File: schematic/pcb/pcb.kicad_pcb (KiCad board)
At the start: 2 copper layers, 23 parts, among them P1 USB_C_Plug_USB2.0, U1 ESP32-WROOM-32, U2 NEO-M9N, U3 CP2102N-Axx-xQFN28

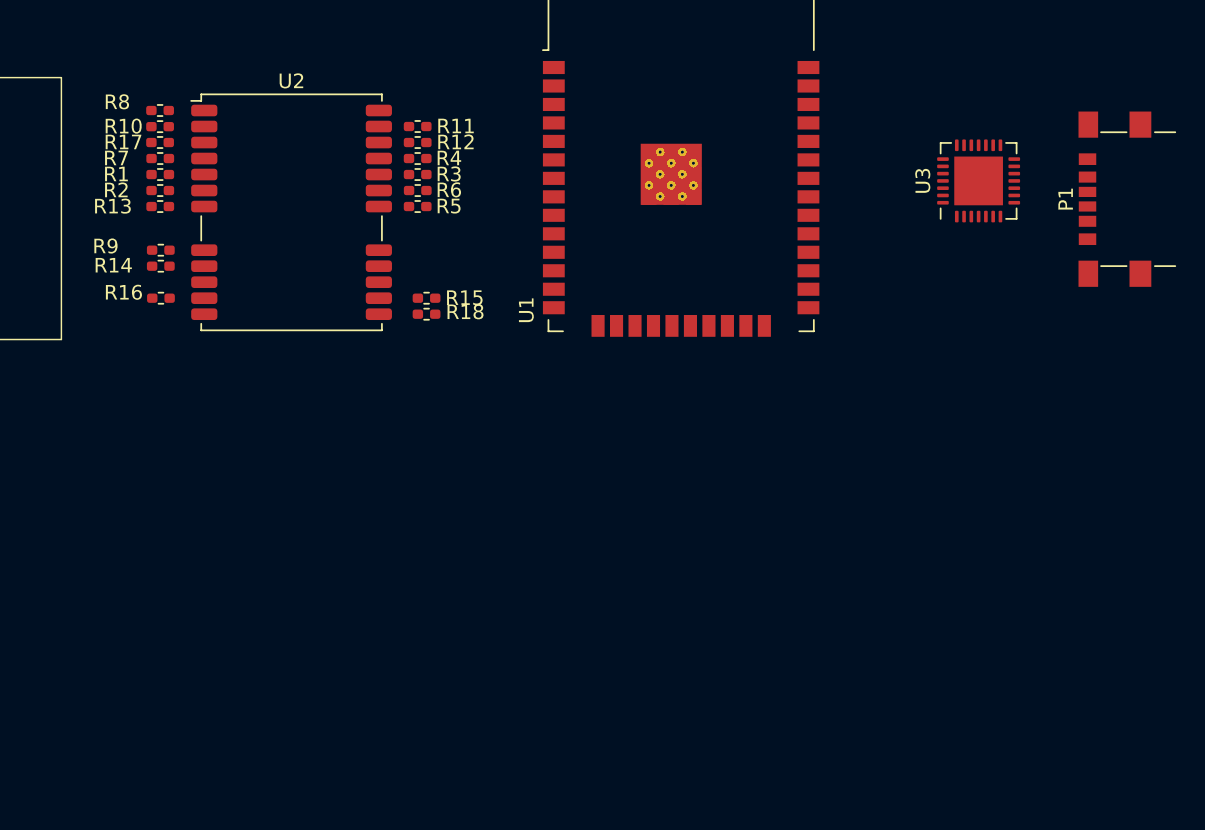
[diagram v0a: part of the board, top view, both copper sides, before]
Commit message: schematic update
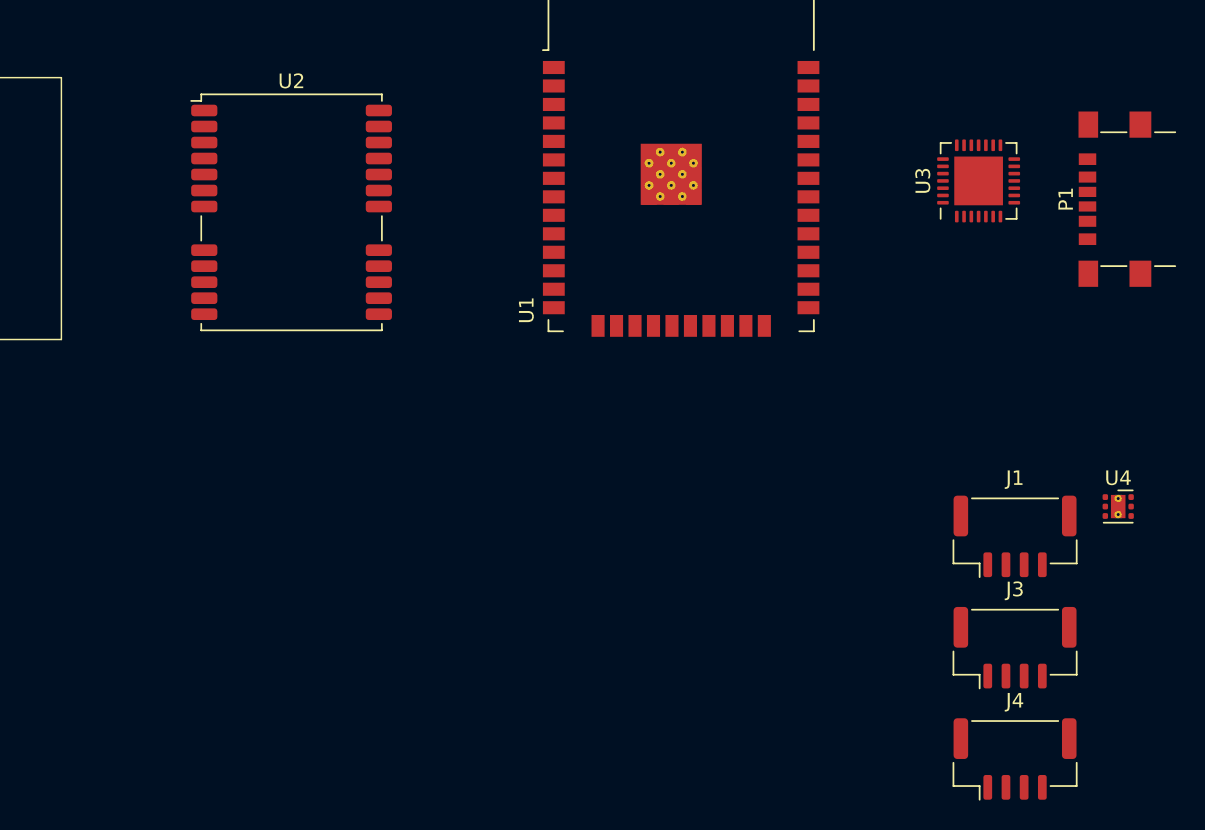
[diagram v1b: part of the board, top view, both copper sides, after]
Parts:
- removed R1, R10, R11, R12, R13, R14, R15, R16, R17, R18, R2, R3, R4, R5, R6, R7, R8, R9: R_Small, Resistor_SMD:R_0402_1005Metric_Pad0.72x0.64mm_HandSolder
- added J1: MAV_Serial, Connector_JST:JST_GH_BM04B-GHS-TBT_1x04-1MP_P1.25mm_Vertical, F.Cu at (179.9, 132.0)
- added J3: SERVO_Serial, Connector_JST:JST_GH_BM04B-GHS-TBT_1x04-1MP_P1.25mm_Vertical, F.Cu at (179.9, 139.6)
- added J4: MAG_Serial, Connector_JST:JST_GH_BM04B-GHS-TBT_1x04-1MP_P1.25mm_Vertical, F.Cu at (179.9, 147.3)
- added U4: LP5912-3.3DRV, Package_SON:WSON-6-1EP_2x2mm_P0.65mm_EP1x1.6mm_ThermalVias, F.Cu at (187.0, 129.9)
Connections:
- net Net-(P1-D+) renamed USB_D+
- net Net-(P1-D-) renamed USB_D-
- C1 pad 1: Net-(C1-Pad1) -> Net-(U2-RF_IN)
- P1 pad A9: Net-(U3-VBUS) -> VBUS
- P1 pad B9: Net-(U3-VBUS) -> VBUS
- U1 pad 13: GPS_MISO -> GPS_SCK
- U1 pad 14: unconnected-(U1-IO12-Pad14) -> GPS_MISO
- U1 pad 16: GPS_SCK -> GPS_MOSI
- U1 pad 2: unconnected-(U1-VDD-Pad2) -> +3V3
- U1 pad 23: unconnected-(U1-IO15-Pad23) -> GPS_CS
- U1 pad 25: unconnected-(U1-IO0-Pad25) -> IO0
- U1 pad 27: GPS_MOSI -> unconnected-(U1-IO16-Pad27)
- U1 pad 29: unconnected-(U1-IO5-Pad29) -> SCREEN_CS
- U1 pad 3: unconnected-(U1-EN-Pad3) -> EN
- U1 pad 30: unconnected-(U1-IO18-Pad30) -> SCREEN_SCK
- U1 pad 31: unconnected-(U1-IO19-Pad31) -> SCREEN_MISO
- U1 pad 37: unconnected-(U1-IO23-Pad37) -> SCREEN_MOSI
- U2 pad 1: Net-(U2-~{SAFEBOOT}) -> unconnected-(U2-~{SAFEBOOT}-Pad1)
- U2 pad 10: Net-(R18-Pad2) -> GND
- U2 pad 12: Net-(R18-Pad2) -> GND
- U2 pad 13: Net-(R18-Pad2) -> GND
- U2 pad 14: Net-(U2-LNA_EN) -> unconnected-(U2-LNA_EN-Pad14)
- U2 pad 18: Net-(U2-SDA/~{SPI_CS}) -> GPS_CS
- U2 pad 19: Net-(U2-SCL/SPI_CLK) -> GPS_SCK
- U2 pad 2: Net-(U2-D_SEL) -> unconnected-(U2-D_SEL-Pad2)
- U2 pad 20: Net-(U2-TXD/SPI_MISO) -> GPS_MISO
- U2 pad 21: Net-(U2-RXD/SPI_MOSI) -> GPS_MOSI
- U2 pad 22: Net-(U2-V_BCKP) -> +3V3
- U2 pad 23: Net-(U2-VCC) -> +3V3
- U2 pad 24: Net-(R18-Pad2) -> GND
- U2 pad 3: Net-(U2-TIMEPULSE) -> unconnected-(U2-TIMEPULSE-Pad3)
- U2 pad 4: Net-(U2-EXTINT) -> unconnected-(U2-EXTINT-Pad4)
- U2 pad 5: Net-(U2-USB_DM) -> unconnected-(U2-USB_DM-Pad5)
- U2 pad 6: Net-(U2-USB_DP) -> unconnected-(U2-USB_DP-Pad6)
- U2 pad 7: Net-(U2-VDD_USB) -> GND
- U2 pad 8: Net-(U2-~{RESET}) -> unconnected-(U2-~{RESET}-Pad8)
- U2 pad 9: Net-(U2-VCC_RF) -> unconnected-(U2-VCC_RF-Pad9)
- U3 pad 1: unconnected-(U3-~{DCD}-Pad1) -> DCD
- U3 pad 11: unconnected-(U3-~{SUSPEND}-Pad11) -> Net-(U3-~{SUSPEND})
- U3 pad 2: unconnected-(U3-~{RI}/CLK-Pad2) -> RI
- U3 pad 23: unconnected-(U3-~{CTS}-Pad23) -> CTS
- U3 pad 24: unconnected-(U3-~{RTS}-Pad24) -> RTS
- U3 pad 27: unconnected-(U3-~{DSR}-Pad27) -> DSR
- U3 pad 28: unconnected-(U3-~{DTR}-Pad28) -> DTR
- U3 pad 7: Net-(U3-VBUS) -> +3V3
- U3 pad 9: unconnected-(U3-~{RST}-Pad9) -> Net-(U3-~{RST})

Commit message: updt
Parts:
- added C10: 0.1uF/50V 10%, Capacitor_SMD:C_0805_2012Metric, F.Cu at (120.1, 148.7)
- added C2: 0.1uF, Capacitor_SMD:C_0805_2012Metric, F.Cu at (128.9, 117.9)
- added C3: 4.7uF, Capacitor_SMD:C_0805_2012Metric, F.Cu at (128.3, 123.6)
- added C4: 10uF, Capacitor_SMD:C_0805_2012Metric, F.Cu at (120.1, 128.6)
- added C5: 0.1uF, Capacitor_SMD:C_0805_2012Metric, F.Cu at (120.1, 131.9)
- added C6: 0.1uF/50V 10%, Capacitor_SMD:C_0805_2012Metric, F.Cu at (120.1, 135.3)
- added C7: 10uF, Capacitor_SMD:C_0805_2012Metric, F.Cu at (107.4, 91.3)
- added C8: 10uF, Capacitor_SMD:C_0805_2012Metric, F.Cu at (114.3, 91.9)
- added C9: 0.1uF/50V 10%, Capacitor_SMD:C_0805_2012Metric, F.Cu at (120.1, 145.3)
- added J2: Display, Connector_JST:JST_GH_BM05B-GHS-TBT_1x05-1MP_P1.25mm_Vertical, F.Cu at (169.1, 132.0)
- added J5: Servo, Connector_JST:JST_GH_BM03B-GHS-TBT_1x03-1MP_P1.25mm_Vertical, F.Cu at (167.8, 139.6)
- added Q1: NPN, Package_TO_SOT_SMD:TSOT-23, F.Cu at (124.4, 103.8)
- added Q2: NPN, Package_TO_SOT_SMD:TSOT-23, F.Cu at (124.4, 108.7)
- added R19: 22.1K 5%, Resistor_SMD:R_0805_2012Metric, F.Cu at (142.5, 132.0)
- added R20: 10K 5%, Resistor_SMD:R_0805_2012Metric, F.Cu at (142.5, 134.9)
- added R21: 10K 5%, Resistor_SMD:R_0805_2012Metric, F.Cu at (142.5, 137.9)
- added R22: 47.5K 5%, Resistor_SMD:R_0805_2012Metric, F.Cu at (142.5, 140.8)
- added R23: 2K 5%, Resistor_SMD:R_0805_2012Metric, F.Cu at (142.5, 143.8)
- added R25: 10K 5%, Resistor_SMD:R_0805_2012Metric, F.Cu at (142.5, 146.8)
- moved P1 94.2 mm to (93.8, 104.4), turned to -90 degrees
- moved U4 84.9 mm to (111.2, 91.6), turned to 180 degrees
- moved U3 69.5 mm to (107.9, 107.1)
- moved C1 41.9 mm to (81.7, 145.0)
- moved U2 41.5 mm to (100.8, 139.0)
- moved U1 12.9 mm to (144.8, 103.8)
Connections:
- U4 pad 4: +5V -> VBUS
- U4 pad 6: +5V -> VBUS

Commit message: pcb updt
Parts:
- added REF**: MountingHole_2.2mm_M2_Pad, MountingHole:MountingHole_2.2mm_M2_Pad, F.Cu at (130.9, 88.6)
- added REF**: MountingHole_2.2mm_M2_Pad, MountingHole:MountingHole_2.2mm_M2_Pad, F.Cu at (180.8, 88.6)
- added REF**: MountingHole_2.2mm_M2_Pad, MountingHole:MountingHole_2.2mm_M2_Pad, F.Cu at (130.9, 138.5)
- added REF**: MountingHole_2.2mm_M2_Pad, MountingHole:MountingHole_2.2mm_M2_Pad, F.Cu at (180.8, 138.5)
- J5: footprint Connector_JST:JST_GH_BM03B-GHS-TBT_1x03-1MP_P1.25mm_Vertical -> Connector_PinHeader_2.54mm:PinHeader_1x03_P2.54mm_Vertical
- moved C1 99.5 mm to (173.6, 106.9), turned to -90 degrees
- moved J3 65.5 mm to (129.2, 98.1), turned to 90 degrees
- moved P1 64.3 mm to (155.7, 87.1), turned to 180 degrees
- moved J4 64.0 mm to (129.3, 108.1), turned to 90 degrees
- moved U2 61.1 mm to (156.0, 112.8), turned to 180 degrees
- moved C7 59.1 mm to (166.5, 92.1)
- moved C8 59.1 mm to (173.4, 92.7)
- moved U4 59.1 mm to (170.3, 92.3)
- moved J5 58.2 mm to (142.6, 87.1), turned to -90 degrees
- moved J1 52.5 mm to (129.3, 118.0), turned to 90 degrees
- moved R25 51.7 mm to (138.2, 95.2), turned to 180 degrees
- moved C10 49.4 mm to (144.4, 105.7), turned to 180 degrees
- moved R23 45.8 mm to (138.2, 98.2), turned to 180 degrees
- moved U3 45.3 mm to (151.9, 96.4), turned to -90 degrees
- moved R21 44.2 mm to (144.7, 93.8), turned to 180 degrees
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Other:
- board outline added: 59.9 x 59.9 mm

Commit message: pcb update
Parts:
- removed the U1 at (155.8, 133.9)
- added ESP1: ESP32-WROOM-32, RF_Module:ESP32-WROOM-32, F.Cu at (176.0, 109.4)
- added J6: 5V, Connector_Wuerth:Wuerth_WR-WTB_64800211622_1x02_P1.50mm_Vertical, F.Cu at (150.0, 87.1)
- added R6: 10K 5% (NC), Resistor_SMD:R_0805_2012Metric, F.Cu at (143.2, 115.4)
- J1: value MAV_Serial -> MAVLINK
- J2: value Display -> DISPLAY
- J3: value SERVO_Serial -> SER. SERVO
- J4: value MAG_Serial -> MAG.
- J5: value Servo -> SERVO
- moved C10 51.6 mm to (184.2, 96.0), turned to 90 degrees
- moved C6 51.5 mm to (182.1, 96.0), turned to 90 degrees
- moved C7 44.4 mm to (177.8, 96.0), turned to 90 degrees
- moved R7 41.7 mm to (179.9, 96.0), turned to -90 degrees
- moved C3 32.8 mm to (152.1, 131.7), turned to 180 degrees
- moved C8 31.8 mm to (173.5, 96.0), turned to -90 degrees
- moved C9 28.4 mm to (171.2, 96.0), turned to -90 degrees
- moved U1 24.5 mm to (175.4, 127.8), turned to 90 degrees
- moved R1 23.1 mm to (154.4, 114.7), turned to 90 degrees
- moved C1 19.6 mm to (148.3, 99.4), turned to -90 degrees
- moved LDO1 19.5 mm to (152.1, 99.4)
- moved C2 18.8 mm to (155.9, 99.5)
- moved R2 17.4 mm to (154.4, 111.1), turned to -90 degrees
- moved CP1 17.2 mm to (148.8, 113.3)
- moved Q2 15.6 mm to (159.1, 110.4)
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- renumbered C7 to C1, C5 to C10, C8 to C2, C1 to C3, C2 to C4, C3 to C5, C4 to C6, C6 to C7, C9 to C8, C10 to C9, U3 to CP1, U4 to LDO1, R21 to R1, R20 to R2, R19 to R3, R22 to R4, R23 to R5, R25 to R7, U2 to U1
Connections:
- J5 pad 1: unconnected-(J5-Pin_1-Pad1) -> GND
- J5 pad 3: unconnected-(J5-Pin_3-Pad3) -> +5V

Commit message: trzymam kciuki
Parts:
- J6: footprint Connector_Wuerth:Wuerth_WR-WTB_64800211622_1x02_P1.50mm_Vertical -> Connector_Amphenol:VI0221550000G
- P1: footprint Connector_USB:USB_C_Receptacle_GCT_USB4135-GF-A_6P_TopMnt_Horizontal -> Connector_USB:USB_C_Receptacle_HRO_TYPE-C-31-M-12
- moved C2 14.3 mm to (142.4, 104.4), turned to 0 degrees
- moved LDO1 8.43 mm to (147.1, 106.2), turned to 0 degrees
- moved C4 5.90 mm to (142.4, 108.6)
- moved C5 5.90 mm to (142.4, 106.5)
- moved J5 4.27 mm to (138.5, 86.0), turned to 0 degrees
- moved J6 3.22 mm to (152.3, 89.4), turned to 180 degrees
- moved C1 2.90 mm to (147.2, 102.1), turned to 180 degrees
- moved P1 1.71 mm to (164.0, 87.3)
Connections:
- J5 pad 3: +5V -> VBUS
- J6 pad 1: +5V -> GND
- J6 pad 2: GND -> VBUS
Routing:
- net VBUS: track 0.00 -> 63.5 mm
- net GPS_MOSI: track 0.00 -> 48.1 mm, vias 0 -> 2
- net EN: track 0.00 -> 39.0 mm, vias 0 -> 2
- net ESP32_RX0: track 0.00 -> 36.0 mm, vias 0 -> 2
- net Net-(U1-RF_IN): track 0.00 -> 32.7 mm
- net ESP32_TX0: track 0.00 -> 32.1 mm, vias 0 -> 2
- net GND: track 0.00 -> 31.1 mm, vias 0 -> 84
- net GPS_MISO: track 0.00 -> 27.8 mm
- net GPS_SCK: track 0.00 -> 27.8 mm
- net USB_D+: track 0.00 -> 26.3 mm
- net USB_D-: track 0.00 -> 25.9 mm
- net +3V3: track 0.00 -> 24.2 mm, vias 0 -> 7
- net GPS_CS: track 0.00 -> 15.4 mm, vias 0 -> 2
- net Net-(Q2-B): track 0.00 -> 15.0 mm
- net IO0: track 0.00 -> 10.8 mm, vias 0 -> 2
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- added copper zone on In2.Cu, net +3V3
- added copper zone on In1.Cu, net GND
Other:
- copper layers 2 -> 4
